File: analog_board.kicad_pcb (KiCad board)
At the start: 2 copper layers, 80 x 80 mm, 54 parts, among them J301 SAMTEC-TSW-105-07-X-D, J302 SAMTEC-TSW-105-07-X-D, J304 SAMTEC-TSW-105-07-X-D, J305 SAMTEC-TSW-105-07-X-D, U1 LM324, U3 AD620, U4 AD620

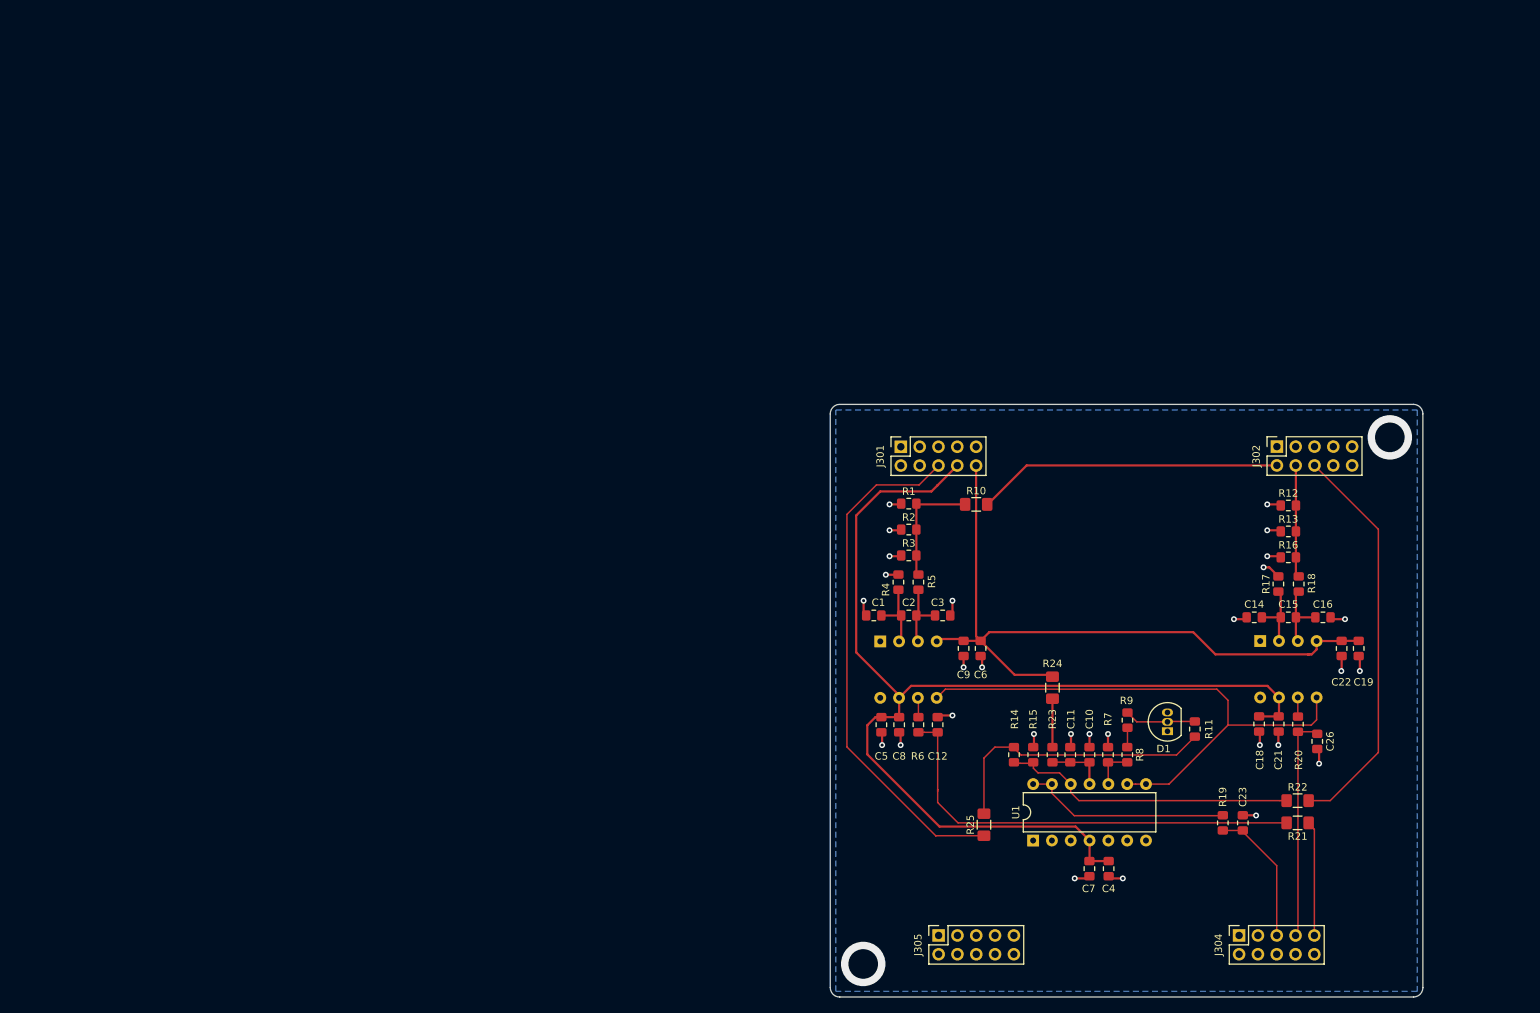
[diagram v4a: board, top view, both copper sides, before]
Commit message: Removed OR jumers. Realigned connectors. Moved large components to Bottom. Thickened tracks.
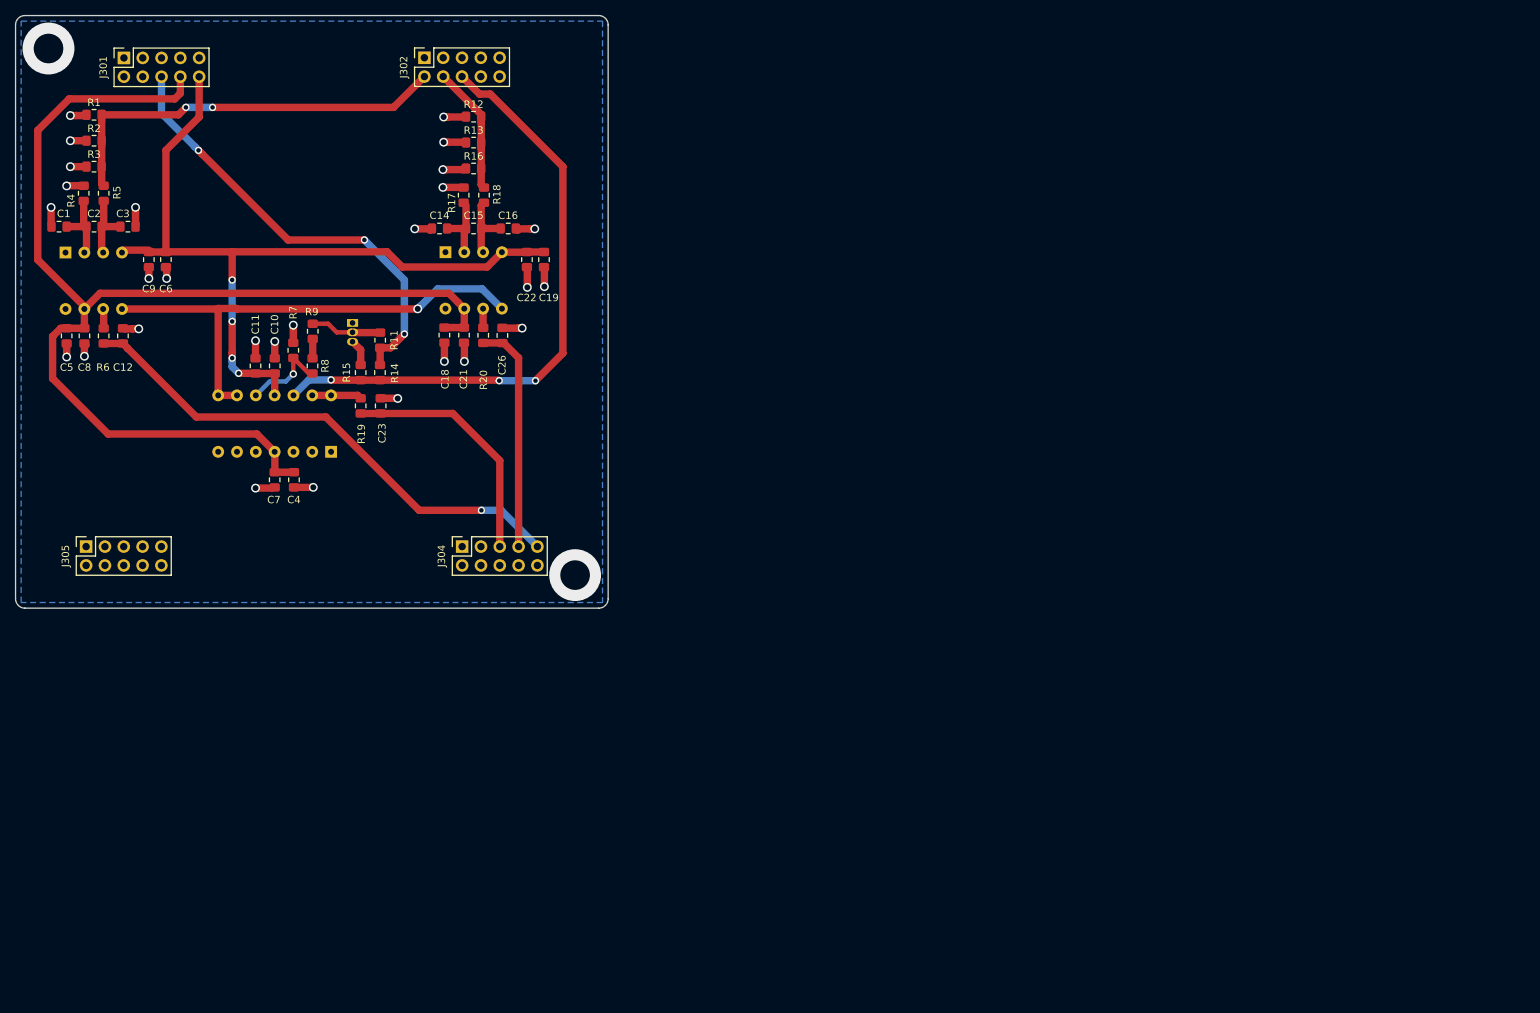
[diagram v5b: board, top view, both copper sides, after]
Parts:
- removed R10, R21, R22, R24, R25: 0R, Resistor_SMD:R_1206_3216Metric_Pad1.42x1.75mm_HandSolder
- removed R23: 0R, Resistor_SMD:R_0805_2012Metric_Pad1.15x1.40mm_HandSolder
- D1, U1: moved to B.Cu
- moved R19 129.3 mm to (46.6, 52.7)
- moved C23 129.3 mm to (49.3, 52.7)
- moved J305 126.5 mm to (9.53, 71.7)
- moved J302 126.5 mm to (55.2, 5.70)
- moved D1 123.1 mm to (45.5, 41.5), turned to 270 degrees
- moved C26 122.9 mm to (65.7, 43.2), turned to 90 degrees
- moved R7 122.8 mm to (37.5, 45.2)
- moved C7 121.9 mm to (35.0, 62.7)
- moved C1 121.9 mm to (5.88, 28.5)
- moved C10 121.9 mm to (35.0, 47.3)
- moved C11 121.9 mm to (32.4, 47.3)
- moved C12 121.9 mm to (14.5, 43.2)
- moved C18 121.9 mm to (57.9, 43.1)
- moved C19 121.9 mm to (71.3, 33.0)
- moved C2 121.9 mm to (10.6, 28.5)
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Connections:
- C12 pad 1: Net-(C12-Pad1) -> /Current_ch1_out
- R1 pad 2: Net-(R1-Pad2) -> /Current_sensor_1
- R14 pad 2: Net-(R14-Pad2) -> /Torque_pedal_in
- R15 pad 1: Net-(R14-Pad2) -> /Torque_pedal_in
- R2 pad 2: Net-(R1-Pad2) -> /Current_sensor_1
- R3 pad 2: Net-(R1-Pad2) -> /Current_sensor_1
- R5 pad 2: Net-(R1-Pad2) -> /Current_sensor_1
- R6 pad 1: Net-(C12-Pad1) -> /Current_ch1_out
- U1 pad 12: Net-(R14-Pad2) -> /Torque_pedal_in
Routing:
- net Net-(C12-Pad1): track 61.0 -> 0.00 mm
- net /Current_ch1_out: track 15.6 -> 69.9 mm, vias 0 -> 1
- net /3V3_REF: track 107.6 -> 60.7 mm, vias 0 -> 3
- net Net-(R14-Pad2): track 40.1 -> 0.00 mm
- net /Torque_pedal_in: track 54.5 -> 82.7 mm, vias 0 -> 3
- net Net-(R19-Pad2): track 28.2 -> 6.70 mm
- net Net-(R1-Pad2): track 16.4 -> 0.00 mm
- net GND: track 54.7 -> 70.2 mm, vias 29 -> 28
- net /Torque_pedal_ADC: track 18.7 -> 33.2 mm
- net /Current_sensor_1: track 41.2 -> 55.5 mm, vias 0 -> 2
- net +15V: track 152.7 -> 160.8 mm
- net /amp_ref: track 76.0 -> 67.9 mm, vias 0 -> 1
- net Net-(R7-Pad1): track 5.41 -> 12.2 mm, vias 0 -> 1
- net /Current_sensor_2: track 15.2 -> 17.3 mm
- net -15V: track 110.1 -> 108.2 mm, vias 0 -> 4
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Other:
- net class Current_sensor: trace_width 0.3 -> 1; via_dia 0.8 -> 1; via_drill 0.4 -> 0.6
- net class Default: trace_width 0.2 -> 0.6; via_dia 0.8 -> 1; via_drill 0.4 -> 0.6
- net class GND added: clearance 0.2, trace_width 1, via_dia 1.2, via_drill 0.8
- net class Power: trace_width 0.3 -> 1; via_dia 0.8 -> 1; via_drill 0.4 -> 0.6
- rule via_min_drill: 0.4 -> 0.6
- rule via_min_size: 0.55 -> 1

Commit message: Added test points and ground fill on top
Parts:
- added C13: 1n, Capacitor_SMD:C_0805_2012Metric_Pad1.15x1.40mm_HandSolder, F.Cu at (54.3, 43.2)
- added C17: 1n, Capacitor_SMD:C_0805_2012Metric_Pad1.15x1.40mm_HandSolder, F.Cu at (19.0, 42.5)
- added TP1: TP_Isense1, TestPoint:TestPoint_2Pads_Pitch2.54mm_Drill0.8mm, B.Cu at (46.8, 12.4)
- added TP10: TP_pedalB, TestPoint:TestPoint_2Pads_Pitch2.54mm_Drill0.8mm, B.Cu at (65.3, 60.0)
- added TP11: TP_ch2_outA, TestPoint:TestPoint_2Pads_Pitch2.54mm_Drill0.8mm, B.Cu at (71.0, 40.0)
- added TP12: TP_ch2_ref, TestPoint:TestPoint_2Pads_Pitch2.54mm_Drill0.8mm, B.Cu at (53.6, 31.8)
- added TP13: TP_ch2_outB, TestPoint:TestPoint_2Pads_Pitch2.54mm_Drill0.8mm, B.Cu at (68.6, 44.7)
- added TP2: TP_A1in, TestPoint:TestPoint_2Pads_Pitch2.54mm_Drill0.8mm, B.Cu at (9.30, 29.2)
- added TP3: TP_ch1_outA, TestPoint:TestPoint_2Pads_Pitch2.54mm_Drill0.8mm, B.Cu at (11.9, 48.4)
- added TP4: TP_ch1_ref, TestPoint:TestPoint_2Pads_Pitch2.54mm_Drill0.8mm, B.Cu at (23.1, 39.6)
- added TP5: TP_ch1_outB, TestPoint:TestPoint_2Pads_Pitch2.54mm_Drill0.8mm, B.Cu at (61.7, 66.8)
- added TP6: TP_Isense2, TestPoint:TestPoint_2Pads_Pitch2.54mm_Drill0.8mm, B.Cu at (66.7, 19.7)
- added TP7: TP_pedal_in, TestPoint:TestPoint_2Pads_Pitch2.54mm_Drill0.8mm, B.Cu at (68.8, 15.3)
- added TP8: TP_A2in, TestPoint:TestPoint_2Pads_Pitch2.54mm_Drill0.8mm, B.Cu at (60.5, 29.3)
- added TP9: TP_pedalA, TestPoint:TestPoint_2Pads_Pitch2.54mm_Drill0.8mm, B.Cu at (51.9, 56.1)
- moved C1 2.00 mm to (5.88, 26.5)
- moved C2 2.00 mm to (10.6, 26.5)
- moved C3 2.00 mm to (15.2, 26.5)
- moved C14 1.90 mm to (57.1, 26.9)
- moved C15 1.90 mm to (61.7, 26.9)
- moved C16 1.90 mm to (66.4, 26.9)
- moved R17 1.20 mm to (60.4, 23.1)
- moved R18 1.20 mm to (63.1, 23.1)
- moved R3 1.10 mm to (10.6, 19.3)
- moved R4 1.00 mm to (9.30, 23.0)
- moved R5 1.00 mm to (12.0, 23.0)
- moved R16 0.90 mm to (61.8, 19.8)
- moved R2 0.50 mm to (10.6, 16.4)
- moved R13 0.40 mm to (61.8, 16.8)
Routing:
- net /amp_ref: track 67.9 -> 80.4 mm
- net Net-(R19-Pad2): track 6.70 -> 18.8 mm
- net Net-(R20-Pad2): track 2.59 -> 12.6 mm
- net Net-(R6-Pad2): track 2.66 -> 11.5 mm
- net /Torque_pedal_in: track 82.7 -> 85.9 mm
- net /Current_ch2_out: track 31.1 -> 33.8 mm
- net /Current_sensor_2: track 17.3 -> 19.9 mm
- net Net-(C1-Pad2): track 9.60 -> 11.7 mm
- net Net-(C2-Pad2): track 9.42 -> 11.5 mm
- net /3V3_REF: track 60.7 -> 59.0 mm
- net Net-(C15-Pad2): track 10.1 -> 11.7 mm
- net Net-(C14-Pad2): track 9.84 -> 11.4 mm
- net GND: track 70.2 -> 71.2 mm, vias 28 -> 70
- net /Current_sensor_1: track 55.5 -> 55.0 mm
- net /Current_ch1_out: vias 1 -> 0
- added copper zone on F.Cu, net GND
